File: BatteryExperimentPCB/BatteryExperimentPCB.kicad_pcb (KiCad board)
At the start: 2 copper layers, 27.8 x 32.5 mm, 32 parts, among them J1 TYPE-C-31-M-12, J2 Conn_01x12_Pin, J3 Conn_01x12_Pin, Q1 DMG1012T, SW1 SW_Push, U1 ATtiny3226-M, U2 USBLC6-2P6, U3 BQ25628RYKR

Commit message: cleanup
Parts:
- turned Q1 to 0 degrees
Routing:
- net GND: track 82.6 -> 84.4 mm, vias 22 -> 28
- net Battery+: track 40.6 -> 39.6 mm
- net PB5: track 19.7 -> 18.8 mm
- net VoltageMonitor: track 8.32 -> 8.87 mm

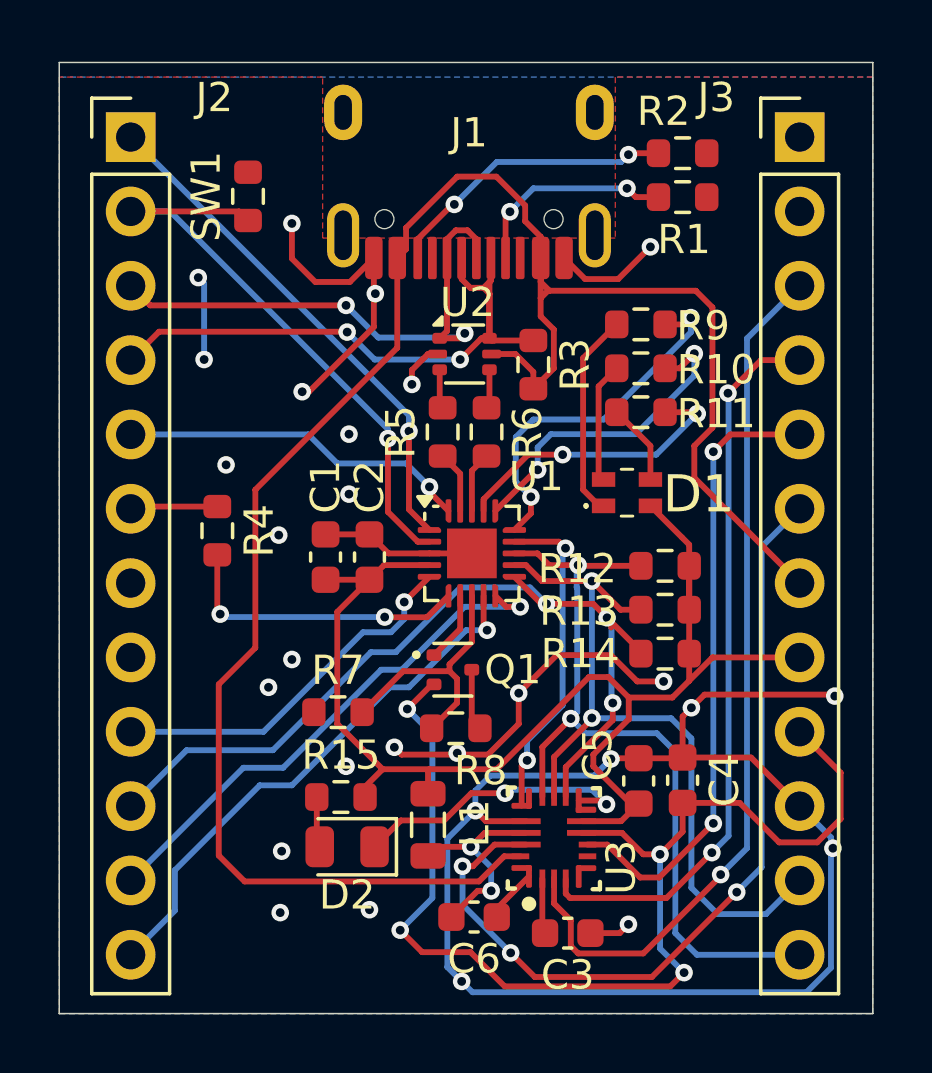
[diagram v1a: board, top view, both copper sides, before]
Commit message: replaced button footprint with one from jlcpcb, moved usb c over to the right to fit button
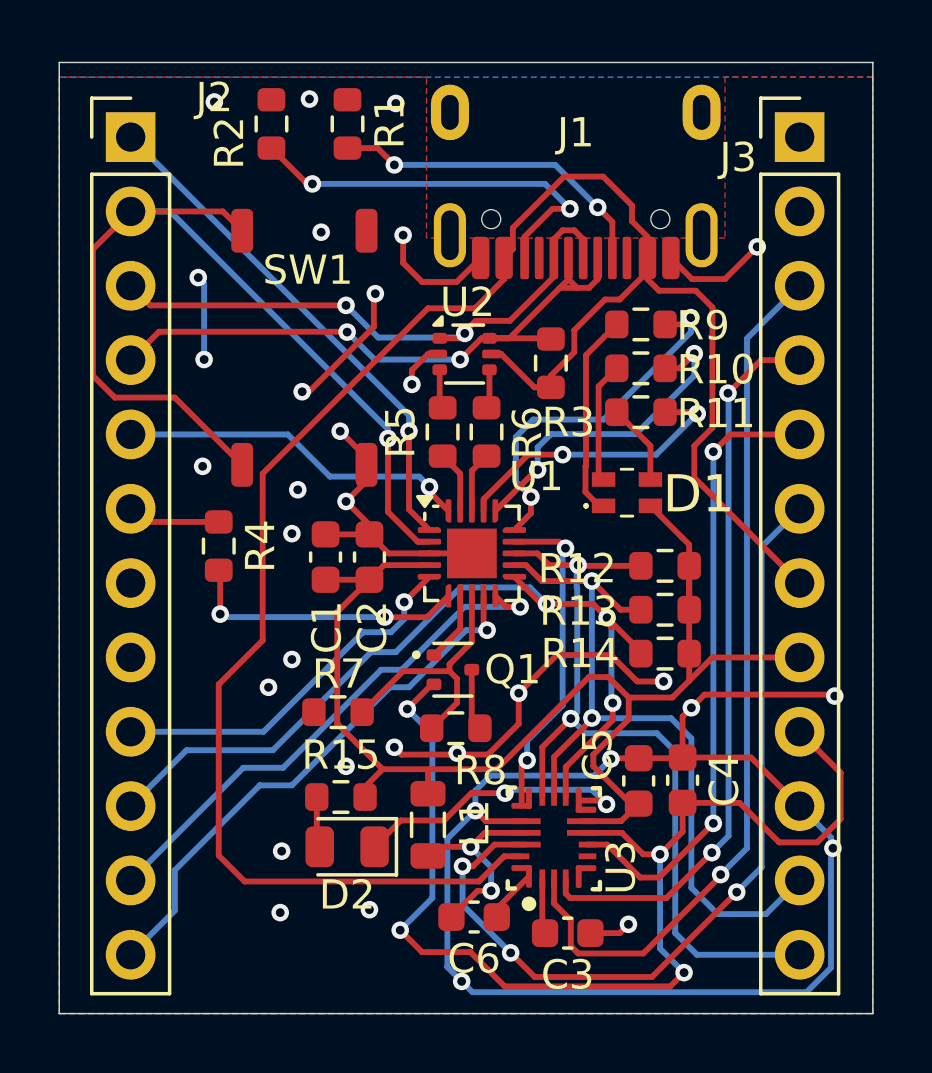
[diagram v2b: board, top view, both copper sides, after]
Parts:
- SW1: value SW_Push -> K2-1157SP; footprint Resistor_SMD:R_0603_1608Metric -> BatteryExperimentPCB:K2-1157SP
- moved R2 14.1 mm to (216.4, 56.5), turned to 90 degrees
- moved R1 11.7 mm to (219.1, 56.5), turned to 90 degrees
- moved SW1 9.18 mm to (215.4, 68.2)
- moved J1 3.65 mm to (226.8, 61.9)
- moved R3 0.60 mm to (226.0, 64.7)
- moved R4 0.53 mm to (214.7, 71.0)
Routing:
- net Button: track 20.7 -> 33.1 mm
- net Net-(J1-CC1): track 7.17 -> 11.3 mm
- net Net-(J1-CC2): track 10.1 -> 13.7 mm
- net GND: track 84.4 -> 87.2 mm, vias 28 -> 33
- net DBUS+: track 18.5 -> 20.2 mm
- net DBUS-: track 21.4 -> 22.3 mm
- net Net-(U1-PA5): track 10.2 -> 9.67 mm

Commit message: cleanup
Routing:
- net DBUS-: track 22.3 -> 23.4 mm
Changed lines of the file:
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@@
+	)
+	(segment
+		(start 225 63.875)
+		(end 225 63.85)
+		(width 0.2)
+		(layer "F.Cu")
+		(net 12)
+	)
+	(segment
+		(start 224.9525 63.8025)
+		(end 224.9525 63.5025)
+		(width 0.2)
+		(layer "F.Cu")
+		(net 12)
 	)
 	(segment
 		(start 219.037696 63.662304)
 		(end 219.025392 63.65)
+		(width 0.2)
+		(layer "F.Cu")
+		(net 12)
+	)
+	(segment
+		(start 225 63.875)
+		(end 225.1 63.875)
+		(width 0.2)
+		(layer "F.Cu")
+		(net 12)
+	)
+	(segment
+		(start 223.9 63.875)
+		(end 225 63.875)
 		(width 0.2)
 		(layer "F.Cu")
@@
 	)
 	(segment
+		(start 224.8525 63.6275)
+		(end 225.1 63.875)
+		(width 0.2)
+		(layer "F.Cu")
+		(net 12)
+	)
+	(segment
 		(start 226.895001 62.15)
 		(end 226.305 62.15)
+		(width 0.2)
+		(layer "F.Cu")
+		(net 12)
+	)
+	(segment
+		(start 224.579999 63.875)
+		(end 224.8025 63.6525)
 		(width 0.2)
 		(layer "F.Cu")
@@
 	)
 	(segment
-		(start 224.579999 63.875)
-		(end 226.2775 62.1775)
-		(width 0.2)
-		(layer "F.Cu")
-		(net 12)
-	)
-	(segment
 		(start 227.6 61.13)
 		(end 227.6 61.854999)
@@
 		(start 226.895001 62.15)
 		(end 226.6 61.854999)
+		(width 0.2)
+		(layer "F.Cu")
+		(net 12)
+	)
+	(segment
+		(start 225.1 63.875)
+		(end 225.975 63.875)
+		(width 0.2)
+		(layer "F.Cu")
+		(net 12)
+	)
+	(segment
+		(start 224.8525 63.6025)
+		(end 224.8525 63.6275)
 		(width 0.2)
 		(layer "F.Cu")
@@
 	)
 	(segment
+		(start 224.8025 63.6525)
+		(end 224.8525 63.6025)
+		(width 0.2)
+		(layer "F.Cu")
+		(net 12)
+	)
+	(segment
 		(start 226.6 61.854999)
 		(end 226.6 61.13)
+		(width 0.2)
+		(layer "F.Cu")
+		(net 12)
+	)
+	(segment
+		(start 225 63.85)
+		(end 224.8025 63.6525)
 		(width 0.2)
 		(layer "F.Cu")
@@
 	)
 	(segment
-		(start 223.9 63.875)
-		(end 225.975 63.875)
+		(start 224.9525 63.5025)
+		(end 226.2775 62.1775)
 		(width 0.2)
 		(layer "F.Cu")
+		(net 12)
+	)
+	(segment
+		(start 224.8525 63.6025)
+		(end 224.9525 63.5025)
+		(width 0.2)
+		(layer "F.Cu")
+		(net 12)
+	)
+	(segment
+		(start 225 63.85)
+		(end 224.9525 63.8025)
+		(width 0.2)
+		(layer "F.Cu")

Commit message: cleanup
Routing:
- net GND: track 87.2 -> 88.5 mm, vias 33 -> 32
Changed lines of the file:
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@@
-	)
-	(via
-		(at 235.636337 81.299055)
-		(size 0.6)
-		(drill 0.3)
-		(layers "F.Cu" "B.Cu")
-		(free yes)
-		(net 1)
 	)
 	(via
@@
 	)
 	(segment
+		(start 229.9 75.6)
+		(end 230.8 76.5)
+		(width 0.2)
+		(layer "B.Cu")
+		(net 1)
+	)
+	(segment
 		(start 228.05 78.25)
 		(end 227.48161 78.81839)
@@
 		(width 0.2)
 		(layer "B.Cu")
+		(net 1)
+	)
+	(segment
+		(start 229.85 75.6)
+		(end 229.9 75.6)
+		(width 0.2)
+		(layer "B.Cu")

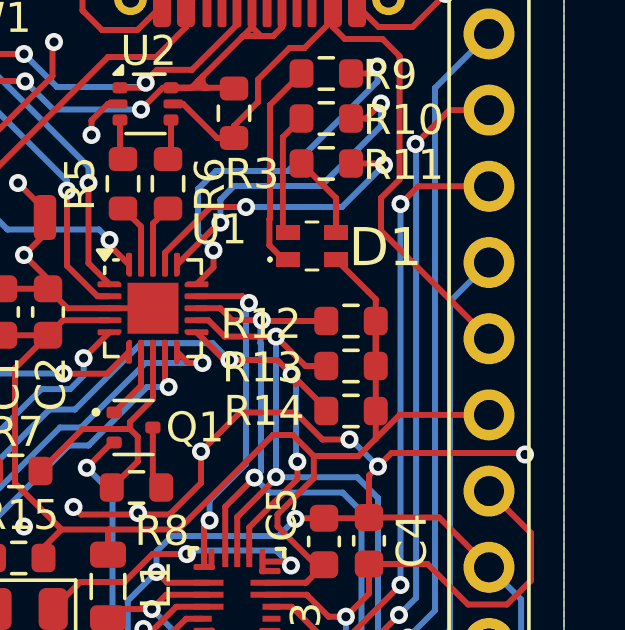
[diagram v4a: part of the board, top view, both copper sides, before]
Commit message: another ground link
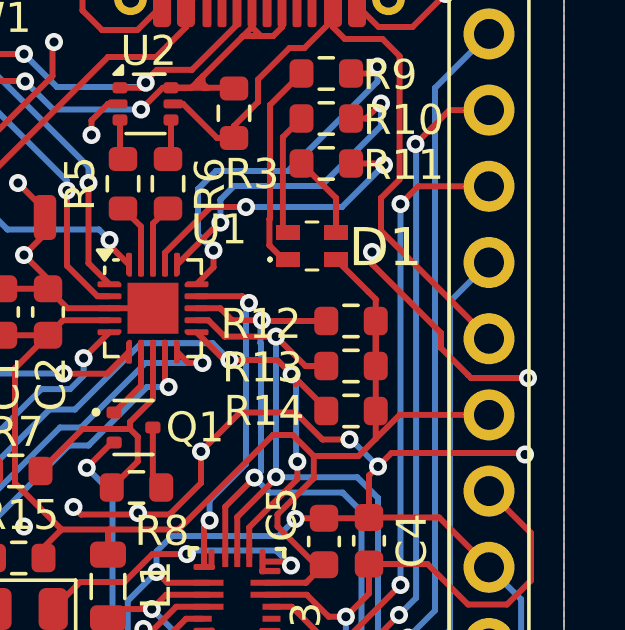
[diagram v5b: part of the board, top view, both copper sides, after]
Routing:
- net GND: track 88.5 -> 96.0 mm, vias 32 -> 34
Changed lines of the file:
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@@
+	)
+	(segment
+		(start 230.6 69.35)
+		(end 230.6 69.75)
+		(width 0.2)
+		(layer "F.Cu")
+		(net 1)
 	)
 	(segment
@@
 	)
 	(segment
+		(start 233.9 73.55)
+		(end 235.8 73.55)
+		(width 0.2)
+		(layer "F.Cu")
+		(net 1)
+	)
+	(segment
 		(start 217.735392 65.7)
 		(end 217.5 65.7)
@@
 	)
 	(segment
+		(start 232.9 72.05)
+		(end 232.9 72.55)
+		(width 0.2)
+		(layer "F.Cu")
+		(net 1)
+	)
+	(segment
 		(start 221.6 61.95)
 		(end 222.78 61.95)
@@
 	)
 	(segment
+		(start 230.6 69.75)
+		(end 232.9 72.05)
+		(width 0.2)
+		(layer "F.Cu")
+		(net 1)
+	)
+	(segment
 		(start 217.5 65.7)
 		(end 217.55 65.7)
@@
 	)
 	(segment
+		(start 233.8 73.45)
+		(end 233.9 73.55)
+		(width 0.2)
+		(layer "F.Cu")
+		(net 1)
+	)
+	(segment
 		(start 218.8 67.05)
 		(end 219.7 67.95)
@@
 	)
 	(segment
+		(start 232.9 72.55)
+		(end 233.8 73.45)
+		(width 0.2)
+		(layer "F.Cu")
+		(net 1)
+	)
+	(segment
 		(start 219.95 63.485392)
 		(end 217.735392 65.7)
@@
 	)
 	(via
+		(at 230.6 69.35)
+		(size 0.6)
+		(drill 0.3)
+		(layers "F.Cu" "B.Cu")
+		(free yes)
+		(net 1)
+	)
+	(via
 		(at 218.8 67.05)
 		(size 0.6)
@@
 		(net 1)
 	)
+	(via
+		(at 235.8 73.55)
+		(size 0.6)
+		(drill 0.3)
+		(layers "F.Cu" "B.Cu")
+		(net 1)
+	)

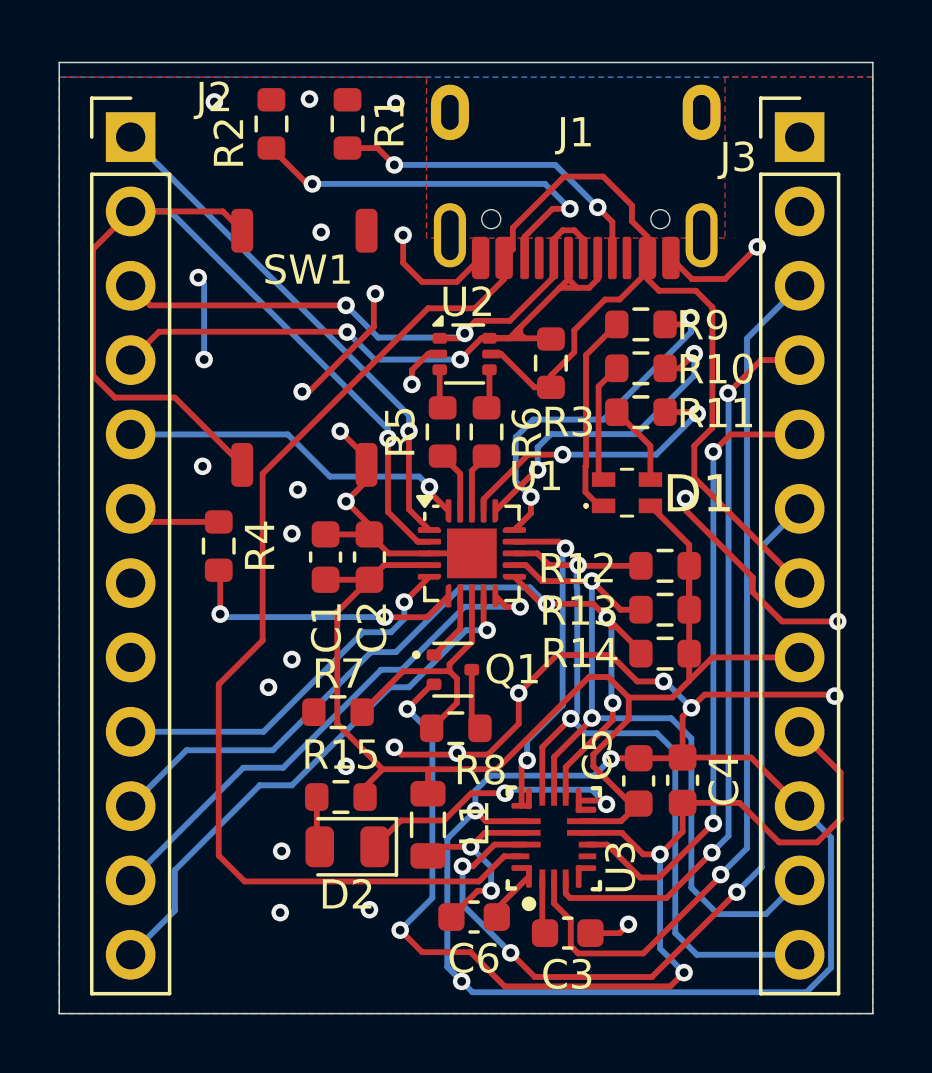
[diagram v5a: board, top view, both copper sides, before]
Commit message: changed led to one with common cathode
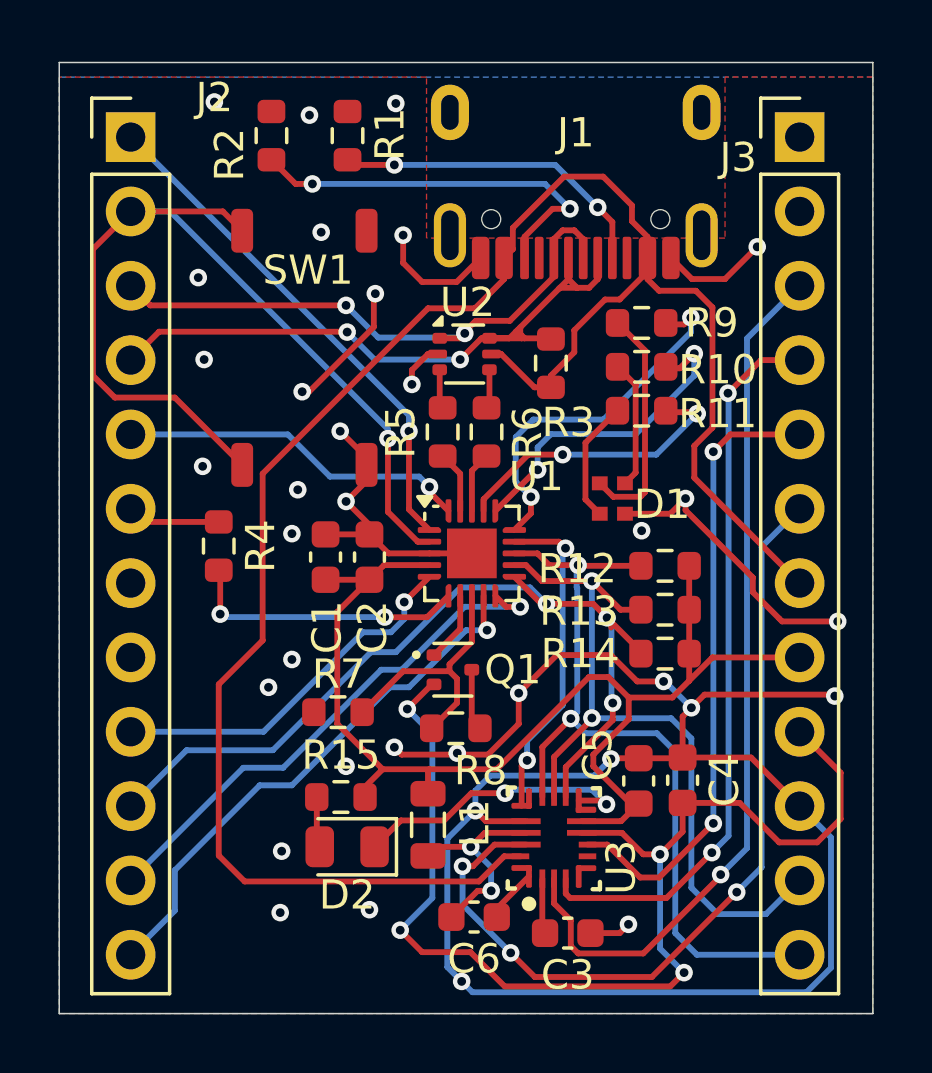
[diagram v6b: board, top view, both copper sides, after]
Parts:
- D1: value LED_ARGB_150066M153000 -> LED_RGBK; footprint BatteryExperimentPCB:150066M153000 -> BatteryExperimentPCB:RS-C1415MBAR
- R10: value 91 -> 47
- R11: value 8.2 -> 56
- R9: value 100 -> 68
- moved D1 0.54 mm to (228.1, 69.3), turned to 90 degrees
- moved R1 0.40 mm to (219.1, 57.0)
- moved R2 0.40 mm to (216.4, 57.0)
- moved R10 0.06 mm to (229.1, 64.8)
- moved R11 0.06 mm to (229.1, 66.3)
- moved R9 0.06 mm to (229.1, 63.4)
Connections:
- D1 pad 1: Net-(D1-RK) -> Net-(D1-GA)
- D1 pad 2: Net-(D1-GK) -> GND
- D1 pad 4: +3.75V -> Net-(D1-RA)
- R10 pad 1: Net-(D1-GK) -> Net-(D1-GA)
- R9 pad 1: Net-(D1-RK) -> Net-(D1-RA)
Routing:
- net Net-(D1-RA): track 0.00 -> 7.97 mm
- net Net-(D1-RK): track 6.99 -> 0.00 mm
- net Net-(D1-GA): track 0.00 -> 4.39 mm
- net Net-(D1-GK): track 4.13 -> 0.00 mm
- net +3.75V: track 44.6 -> 41.0 mm
- net Net-(D1-BA): track 2.78 -> 4.18 mm
- net GND: track 96.0 -> 95.4 mm, vias 34 -> 35
